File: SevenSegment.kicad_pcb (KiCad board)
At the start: 2 copper layers, 33.8 x 131 mm, 72 parts, among them J1 Conn_02x04_Odd_Even, SW2 SW_Push, U1 W25Q16JVUXIQ, U10 VDMR10A1, U11 VDMR10A1, U12 VDMR10A1, U2 RP2040, U3 IS31FL3729-QFLS4-TR, U4 VDMR10A1, U5 VDMR10A1, U6 VDMR10A1, U7 VDMR10A1, U8 VDMR10A1, U9 VDMR10A1, Y1 12.000MHz

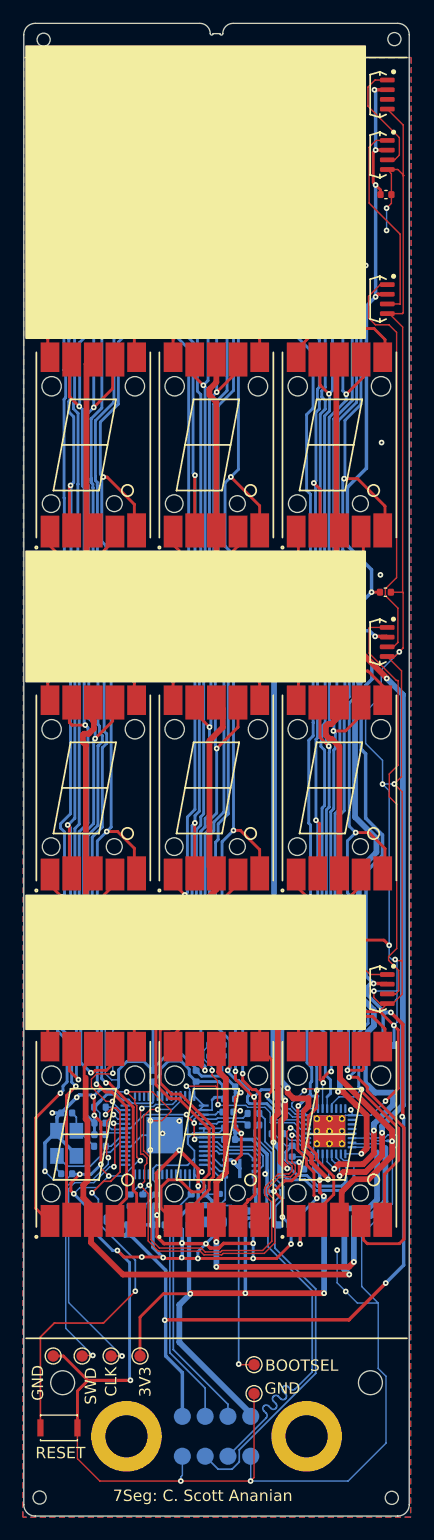
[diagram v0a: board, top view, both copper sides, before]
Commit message: Update design
New features:
* Power switch for NEOPIXEL to save power when sleeping
* Level translator from 3.3V to 5V for neopixel for hygiene
* Use "real" DIP switch footprint for debug/boot buttons, even
  if this is going to be unpopulated in practice, since both
  these modes can be entered via software.  Still can be populated
  for debugging!
* Removed unnecessary RESET switch footprint.

Some additional notes added to v1-notes.txt about other tweaks that
might still be needed before a v2.
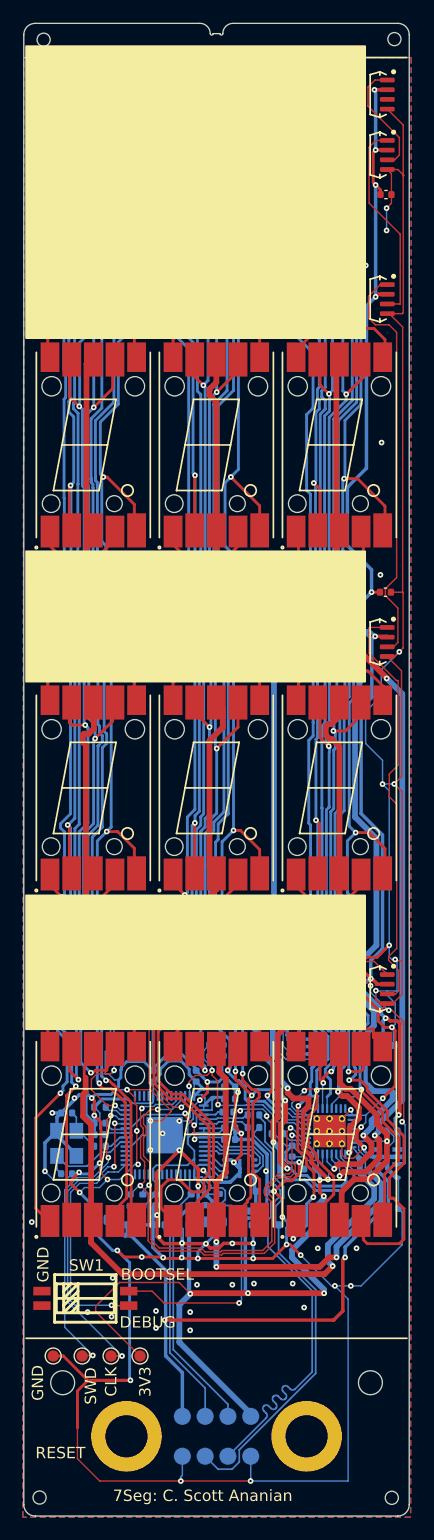
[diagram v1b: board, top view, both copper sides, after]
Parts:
- removed SW2: SW_Push, Button_Switch_SMD:SW_SPST_CK_KXT3
- removed TP5: BOOTSEL, TestPoint:TestPoint_Pad_D1.0mm
- removed TP6: GND, TestPoint:TestPoint_Pad_D1.0mm
- added C23: 1uF, Capacitor_SMD:C_0402_1005Metric, B.Cu at (82.4, 154.0)
- added C24: 100nF, Capacitor_SMD:C_0402_1005Metric, B.Cu at (82.3, 147.2)
- added SW1: DSHP02TSGET, LCSC:SW-SMD_4P_DSHP02TSGET, F.Cu at (55.4, 161.9)
- added U13: 74LVC1G34GW,125, LCSC:SOT-353_L2.1-W1.3-P0.65-LS2.3-BR, B.Cu at (74.3, 139.8)
- added U14: SIP32431DR3-T1GE3, LCSC:SOT-363_L2.0-W1.3-P0.65-LS2.1-BR, B.Cu at (81.9, 149.5)
- moved R5 0.22 mm to (70.2, 146.9)
- moved R6 0.13 mm to (70.2, 145.8)
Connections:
- C20 pad 1: +5V -> +5VP
- C21 pad 1: +5V -> +5VP
- C22 pad 1: +5V -> +5VP
- D10 pad 3: +5V -> +5VP
- D6 pad 3: +5V -> +5VP
- D7 pad 3: +5V -> +5VP
- D8 pad 3: +5V -> +5VP
- D9 pad 3: +5V -> +5VP
- R1 pad 1: Net-(R1-Pad1) -> /BOOTSEL
- U2 pad 15: unconnected-(U2-GPIO12-Pad15) -> /DEBUG_SW
- U2 pad 27: /NEOPIXEL -> /NEOPIXEL_3V3
- U2 pad 40: unconnected-(U2-GPIO28_ADC2-Pad40) -> /NEOPIXEL_PWR
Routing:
- net +5VP: track 0.00 -> 124.9 mm, vias 0 -> 10
- net +5V: track 166.5 -> 52.6 mm, vias 11 -> 2
- net /NEOPIXEL_PWR: track 0.00 -> 51.4 mm, vias 0 -> 6
- net /RUN: track 41.0 -> 2.00 mm, vias 3 -> 0
- net /NEOPIXEL_3V3: track 0.00 -> 36.9 mm, vias 0 -> 4
- net /DEBUG_SW: track 0.00 -> 20.6 mm, vias 0 -> 1
- net /NEOPIXEL: track 38.2 -> 18.0 mm, vias 5 -> 1
- net /BOOTSEL: track 0.00 -> 18.5 mm, vias 0 -> 1
- net GND: track 507.6 -> 525.8 mm, vias 60 -> 84
- net Net-(R1-Pad1): track 15.2 -> 0.00 mm, vias 1 -> 0
- net +3V3: track 124.7 -> 136.9 mm
- net /Driver/LED_SW6: track 57.4 -> 53.5 mm
- net /Driver/LED_SW7: track 47.2 -> 43.7 mm
- net /QSPI_SS: track 6.81 -> 10.1 mm
- net /Driver/CS2: track 313.1 -> 314.5 mm
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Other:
- board text added: "DEBUG"

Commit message: Push 7-segment displays to 0.1mm spacing to allow 2mm min bezel width
We want to try using a PCB as the legend shadow mask, and JLCPCB requires
a minimum PCB width of 2mm to avoid breakage during routing.  That would
also make our 3d-printed spacer more printable as well, win-win.  Hopefully
this will still pass JLCPCB's assembly clearances, otherwise I'm stenciling
these all myself.
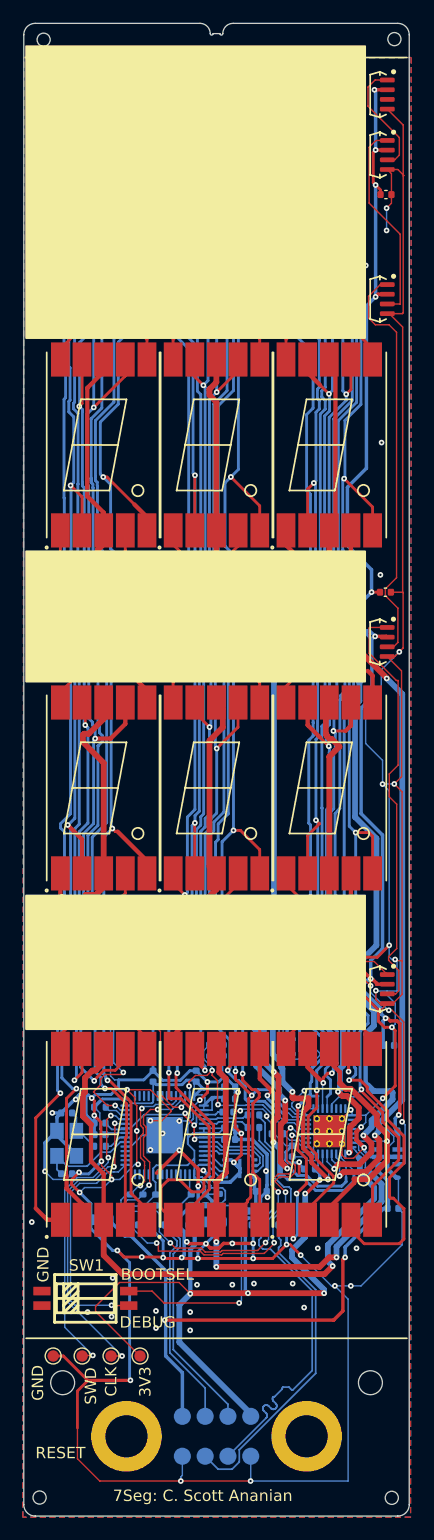
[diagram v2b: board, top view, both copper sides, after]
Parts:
- U10, U11, U12, U4, U5, U6, U7, U8, U9: footprint LEDMatrix:SON_R10A1_VIS_mod -> LEDMatrix:SON_R10A1_VIS_mod_noholes
- moved U10 0.91 mm to (57.0, 147.5)
- moved U4 0.91 mm to (57.0, 87.0)
- moved U7 0.91 mm to (57.0, 117.1)
- moved U12 0.89 mm to (76.8, 147.5)
- moved U6 0.89 mm to (76.8, 87.0)
- moved U9 0.89 mm to (76.8, 117.1)
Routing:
- net GND: track 525.8 -> 506.6 mm, vias 84 -> 82
- net /Driver/LED_SW4: track 57.9 -> 60.8 mm, vias 1 -> 3
- net /Driver/CS4: track 298.7 -> 296.0 mm
- net /Driver/LED_SW3: track 61.7 -> 63.7 mm
- net /USB_DP: track 39.5 -> 37.7 mm
- net /I2C1_SCL: track 42.0 -> 43.7 mm, vias 3 -> 6
- net +3V3: track 136.9 -> 135.3 mm
- net /Driver/CS6: track 256.9 -> 255.3 mm
- net /I2C1_SDA: track 42.4 -> 43.9 mm, vias 3 -> 6
- net /Driver/CS0: track 274.5 -> 275.9 mm
- net /Driver/CS7: track 318.7 -> 317.8 mm
- net /Driver/CS2: track 314.5 -> 315.3 mm
- net /Driver/LED_SW8: track 22.6 -> 23.4 mm
- net /USB_DN: track 39.6 -> 40.3 mm
- net /Driver/LED_SW0: track 90.7 -> 91.3 mm
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
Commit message: Switch from sidelight LEDs for labels to backlight LEDs
I'm not certain there's enough distance for proper diffusion, but
let's try it.  The sidelight LEDs leaked light everywhere and we're
bright enough on the left-hand side.
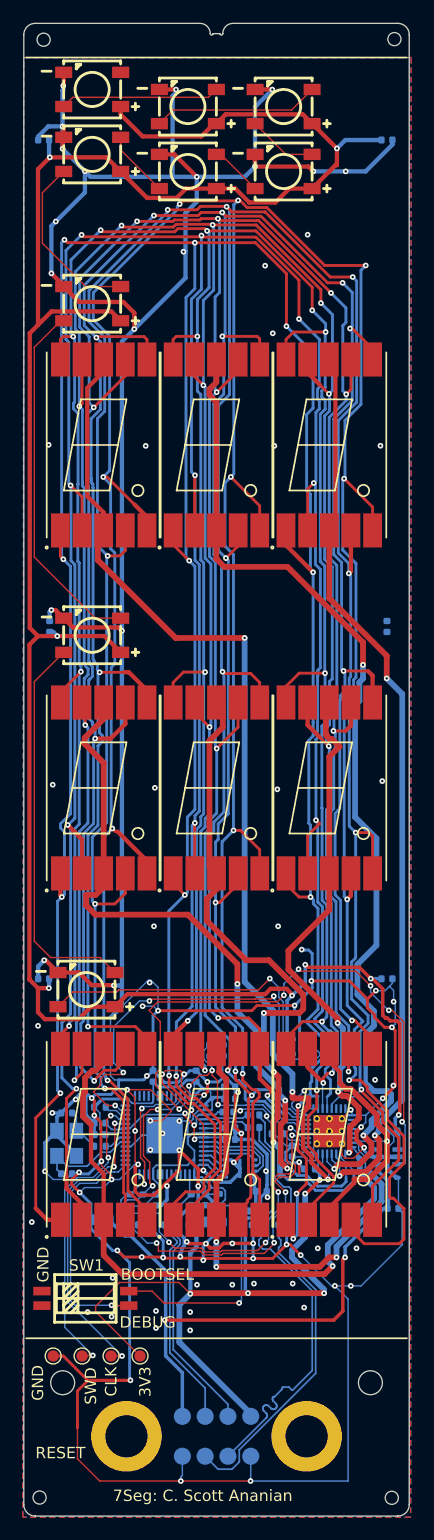
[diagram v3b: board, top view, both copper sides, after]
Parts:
- removed D10, D6, D7, D8, D9: WS2812B-4020, LEDMatrix:WS2812B-4020
- added C25: 100nF, Capacitor_SMD:C_0402_1005Metric, B.Cu at (81.9, 60.2)
- added C26: 100nF, Capacitor_SMD:C_0402_1005Metric, B.Cu at (81.9, 133.8)
- added C27: 100nF, Capacitor_SMD:C_0402_1005Metric, B.Cu at (81.9, 102.9)
- added LED1: XL-5050RGBC-WS2812B, LCSC:LED-SMD_4P-L5.0-W5.0-BL_XL-5050RGBC, F.Cu at (55.5, 134.8)
- added LED2: XL-5050RGBC-WS2812B, LCSC:LED-SMD_4P-L5.0-W5.0-BL_XL-5050RGBC, F.Cu at (56.0, 103.7)
- added LED3: XL-5050RGBC-WS2812B, LCSC:LED-SMD_4P-L5.0-W5.0-BL_XL-5050RGBC, F.Cu at (56.0, 74.6)
- added LED4: XL-5050RGBC-WS2812B, LCSC:LED-SMD_4P-L5.0-W5.0-BL_XL-5050RGBC, F.Cu at (56.0, 61.5)
- added LED5: XL-5050RGBC-WS2812B, LCSC:LED-SMD_4P-L5.0-W5.0-BL_XL-5050RGBC, F.Cu at (64.4, 63.0)
- added LED6: XL-5050RGBC-WS2812B, LCSC:LED-SMD_4P-L5.0-W5.0-BL_XL-5050RGBC, F.Cu at (72.8, 63.0)
- added LED7: XL-5050RGBC-WS2812B, LCSC:LED-SMD_4P-L5.0-W5.0-BL_XL-5050RGBC, F.Cu at (72.8, 57.3)
- added LED8: XL-5050RGBC-WS2812B, LCSC:LED-SMD_4P-L5.0-W5.0-BL_XL-5050RGBC, F.Cu at (64.4, 57.3)
- added LED9: XL-5050RGBC-WS2812B, LCSC:LED-SMD_4P-L5.0-W5.0-BL_XL-5050RGBC, F.Cu at (56.0, 55.8)
- C21, C22: moved to B.Cu
- moved C20 30.8 mm to (51.7, 133.8), turned to 180 degrees
- moved C21 30.4 mm to (51.7, 60.2), turned to 180 degrees
- moved C22 29.6 mm to (52.3, 102.9), turned to 90 degrees
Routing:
- net +5VP: track 124.9 -> 209.2 mm, vias 10 -> 8
- net GND: track 506.6 -> 576.8 mm, vias 82 -> 113
- net Net-(D6-DO): track 37.0 -> 0.00 mm
- net Net-(D7-DO): track 36.1 -> 0.00 mm
- net Net-(LED1-DOU): track 0.00 -> 34.6 mm
- net Net-(LED2-DOU): track 0.00 -> 31.8 mm
- net /Driver/CS3: track 301.9 -> 322.3 mm
- net /Driver/CS6: track 255.3 -> 274.2 mm
- net Net-(D8-DO): track 17.8 -> 0.00 mm
- net /Driver/CS4: track 296.0 -> 313.3 mm
- net /Driver/CS5: track 260.1 -> 276.8 mm
- net /Driver/CS1: track 274.4 -> 291.1 mm
- net /Driver/CS0: track 275.9 -> 292.0 mm
- net Net-(LED3-DOU): track 0.00 -> 15.5 mm
- net /Driver/CS2: track 315.3 -> 330.5 mm
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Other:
- board text added: "7-Segment Input Module 2023 Framework CC BY 4.0 2024 C. Scott Ananian 2024-07-13"
- board text removed: "7-Segment Input Module 2023 Framework CC BY 4.0 2024 C. Scott Ananian 2024-06-23"
